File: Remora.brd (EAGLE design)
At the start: 86.4 x 66.7 mm, 80 parts, among them IC1 MCP23017, J2 GROVE-I2C, P1 PADSMALL, T1 2N3904, T2 BSS138

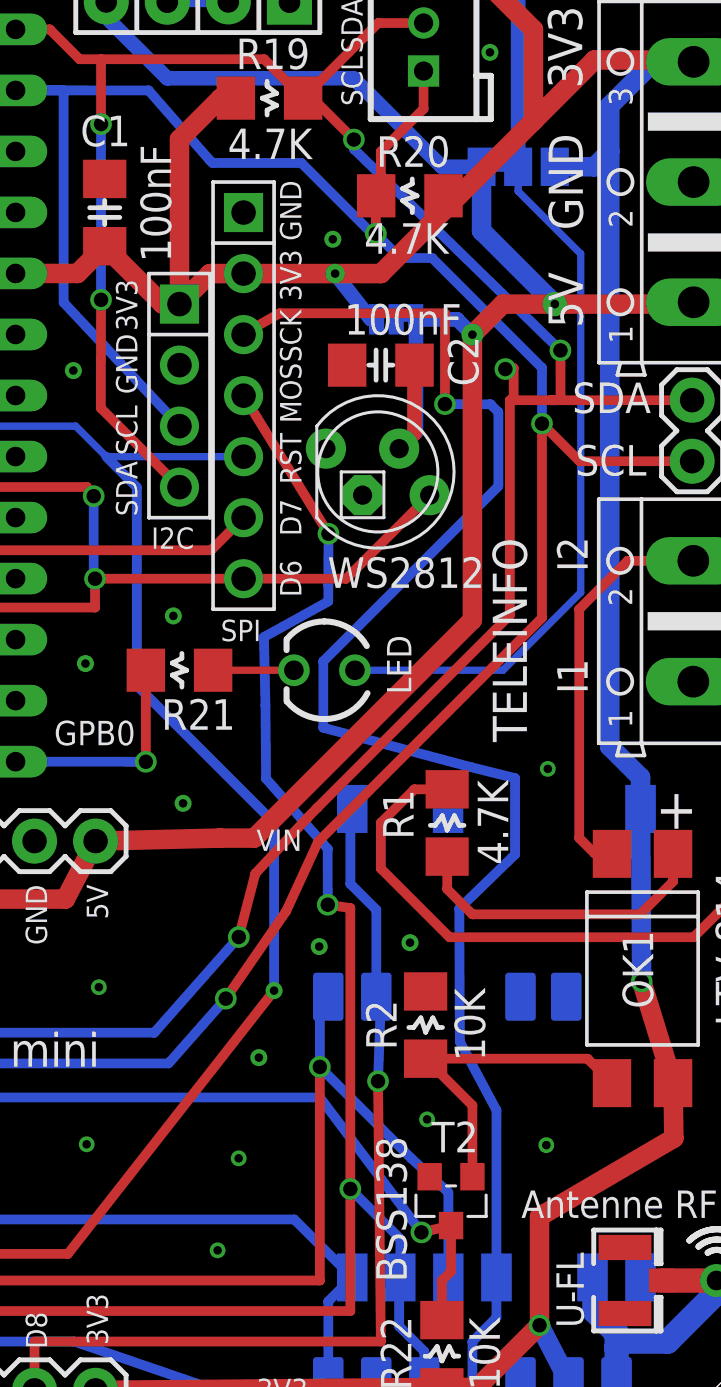
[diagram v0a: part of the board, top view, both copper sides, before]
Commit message: Modification pour export gerbers
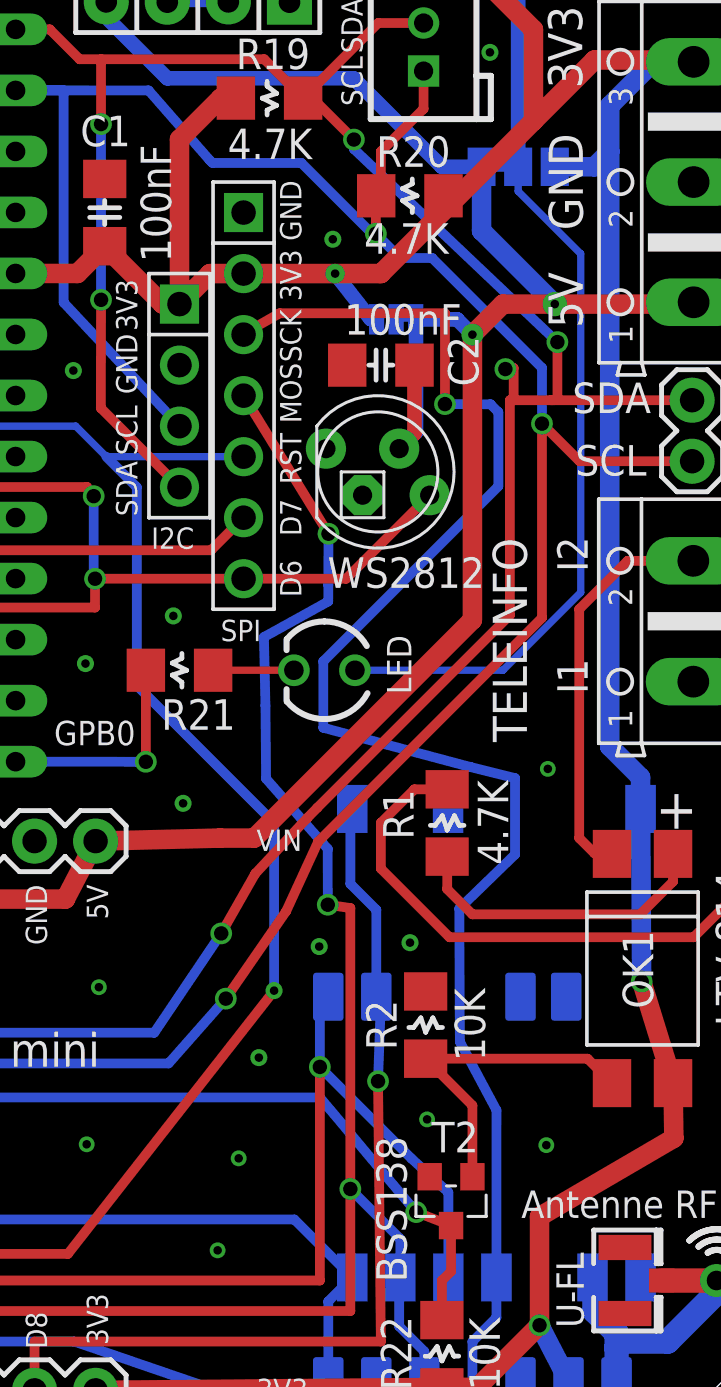
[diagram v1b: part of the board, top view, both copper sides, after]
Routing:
- net RX: track 44.6 -> 44.1 mm
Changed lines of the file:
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@@
 </class>
 </classes>
-<designrules name="ElectroDragon_2layer_DRU_no_angle_20140221">
+<designrules name="SeeedStudio_2layer_DRU_no_angle_20140221">
 <description language="de">&lt;b&gt;EAGLE Design Rules&lt;/b&gt;
 &lt;p&gt;
@@
 <param name="mdPadVia" value="6mil"/>
 <param name="mdViaVia" value="6mil"/>
-<param name="mdSmdPad" value="6mil"/>
-<param name="mdSmdVia" value="6mil"/>
-<param name="mdSmdSmd" value="6mil"/>
+<param name="mdSmdPad" value="0mil"/>
+<param name="mdSmdVia" value="0mil"/>
+<param name="mdSmdSmd" value="0mil"/>
 <param name="mdViaViaSameLayer" value="8mil"/>
 <param name="mnLayersViaInSmd" value="2"/>
-<param name="mdCopperDimension" value="8mil"/>
-<param name="mdDrill" value="6mil"/>
+<param name="mdCopperDimension" value="10mil"/>
+<param name="mdDrill" value="10mil"/>
 <param name="mdSmdStop" value="0mil"/>
 <param name="msWidth" value="6mil"/>
 <param name="msDrill" value="12mil"/>
-<param name="msMicroVia" value="10mm"/>
+<param name="msMicroVia" value="12mil"/>
 <param name="msBlindViaRatio" value="0.5"/>
 <param name="rvPadTop" value="0.25"/>
@@
 <param name="mvStopFrame" value="1"/>
 <param name="mvCreamFrame" value="0"/>
-<param name="mlMinStopFrame" value="4mil"/>
-<param name="mlMaxStopFrame" value="4mil"/>
+<param name="mlMinStopFrame" value="2mil"/>
+<param name="mlMaxStopFrame" value="2mil"/>
 <param name="mlMinCreamFrame" value="0mil"/>
 <param name="mlMaxCreamFrame" value="0mil"/>
@@
 <wire x1="46.5455" y1="18.7831875" x2="49.001890625" y2="16.664675" width="0.4064" layer="16"/>
 <wire x1="49.001890625" y1="16.664675" x2="59.149790625" y2="16.664675" width="0.4064" layer="16"/>
-<via x="62.6667375" y="20.64644375" extent="1-16" drill="0.6" shape="square"/>
-<wire x1="62.6667375" y1="20.64644375" x2="63.354846875" y2="23.28766875" width="0.4064" layer="1"/>
+<via x="61.934796875" y="20.79660625" extent="1-16" drill="0.6" shape="square"/>
+<wire x1="61.934796875" y1="20.79660625" x2="63.354846875" y2="23.28766875" width="0.4064" layer="1"/>
 <wire x1="63.354846875" y1="23.28766875" x2="65.520815625" y2="25.604878125" width="0.4064" layer="1"/>
 <wire x1="65.520815625" y1="25.604878125" x2="65.93389375" y2="26.0263875" width="0.4064" layer="1"/>
@@
 <via x="67.457496875" y="53.839228125" extent="1-16" drill="0.6" shape="square"/>
 <wire x1="67.457496875" y1="53.839228125" x2="67.457496875" y2="53.444290625" width="0.4064" layer="16"/>
-<wire x1="67.457496875" y1="53.444290625" x2="76.0553125" y2="45.062071875" width="0.4064" layer="16"/>
-<via x="76.0553125" y="45.062071875" extent="1-16" drill="0.6" shape="square"/>
-<wire x1="76.0553125" y1="45.062071875" x2="76.05858125" y2="42.99329375" width="0.4064" layer="1"/>
-<wire x1="76.05858125" y1="42.99329375" x2="75.662665625" y2="42.9895" width="0.4064" layer="1"/>
+<wire x1="67.457496875" y1="53.444290625" x2="75.927121875" y2="45.4089625" width="0.4064" layer="16"/>
+<via x="75.927121875" y="45.4089625" extent="1-16" drill="0.6" shape="square"/>
+<wire x1="75.927121875" y1="45.4089625" x2="75.927121875" y2="42.99329375" width="0.4064" layer="1"/>
+<wire x1="75.927121875" y1="42.99329375" x2="75.662665625" y2="42.9895" width="0.4064" layer="1"/>
 <via x="73.761565625" y="44.286565625" extent="1-16" drill="0.6" shape="square"/>
 <wire x1="73.761565625" y1="44.286565625" x2="74.105953125" y2="44.330553125" width="0.4064" layer="1"/>
 <wire x1="74.105953125" y1="44.330553125" x2="74.105953125" y2="42.9895" width="0.4064" layer="1"/>
-<wire x1="59.149790625" y1="16.664675" x2="62.6667375" y2="20.64644375" width="0.4064" layer="16"/>
+<wire x1="59.149790625" y1="16.664675" x2="61.934796875" y2="20.79660625" width="0.4064" layer="16"/>
 <wire x1="60.198" y1="39.37" x2="56.92485625" y2="42.66173125" width="0.4064" layer="1"/>
 <wire x1="56.92485625" y1="42.66173125" x2="56.9326" y2="47.167721875" width="0.4064" layer="1"/>
@@
 <wire x1="41.4655" y1="18.7831875" x2="46.99" y2="13.97" width="0.4064" layer="16"/>
 <wire x1="46.99" y1="13.97" x2="66.04" y2="13.97" width="0.4064" layer="16"/>
-<wire x1="66.04" y1="13.97" x2="70.268128125" y2="8.35275" width="0.4064" layer="16"/>
-<wire x1="70.268128125" y1="8.35275" x2="71.501" y2="8.636" width="0.4064" layer="1"/>
+<wire x1="66.04" y1="13.97" x2="70.049446875" y2="9.19735" width="0.4064" layer="16"/>
+<wire x1="70.049446875" y1="9.19735" x2="71.501" y2="8.636" width="0.4064" layer="1"/>
 <wire x1="71.501" y1="8.636" x2="71.501" y2="6.731" width="0.4064" layer="1"/>
 <wire x1="71.501" y1="6.731" x2="71.12" y2="6.35" width="0.4064" layer="1"/>
 <wire x1="71.12" y1="6.35" x2="71.12" y2="4.702" width="0.4064" layer="1"/>
-<via x="70.268128125" y="8.35275" extent="1-16" drill="0.6" shape="square"/>
+<via x="70.049446875" y="9.19735" extent="1-16" drill="0.6" shape="square"/>
 </signal>
 <signal name="N$16">
